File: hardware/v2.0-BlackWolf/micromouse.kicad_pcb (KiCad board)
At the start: 2 copper layers, 100 x 74 mm, 108 parts, among them CN1 6_PIN_HEADER, CN2 6_PIN_HEADER, M1 MOTOR_MOUNTS_AND_ENCODERS, M2 LEFT_MOTOR, M3 2.54MM-SLIDE-SWITCH_TS02_SWIT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, M4 RIGHT_MOTOR, P1 B3B-PH-SM4-TB, P2 B3B-PH-SM4-TB, Q1 DMN3150LW, Q2 DMN3150LW, Q3 DMN3150LW, Q4 DMN3150LW, Q5 TEFT4300, Q6 TEFT4300, Q7 TEFT4300, Q8 TEFT4300, SW1 SWITCH_DPST, SW2 SWITCH_DPST, SW3 SWITCH_DPST, U1 STM32F446RE_LQFP64, U10 MPU-9250, U11 TPS76850, U12 TPS73633, U2 MAX14871, U3 MAX14871, U9 HCMS-2901

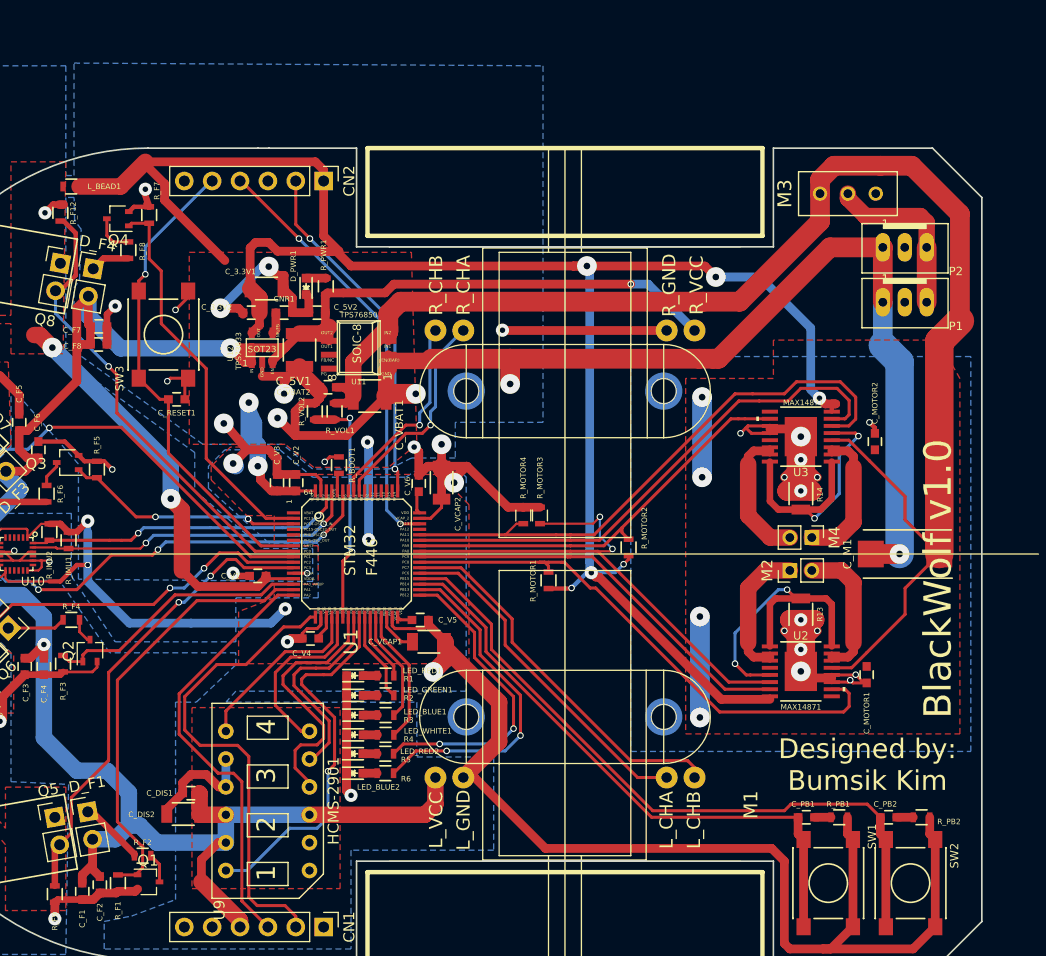
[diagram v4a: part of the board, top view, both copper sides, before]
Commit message: PCB: Separated 5V source due to heat
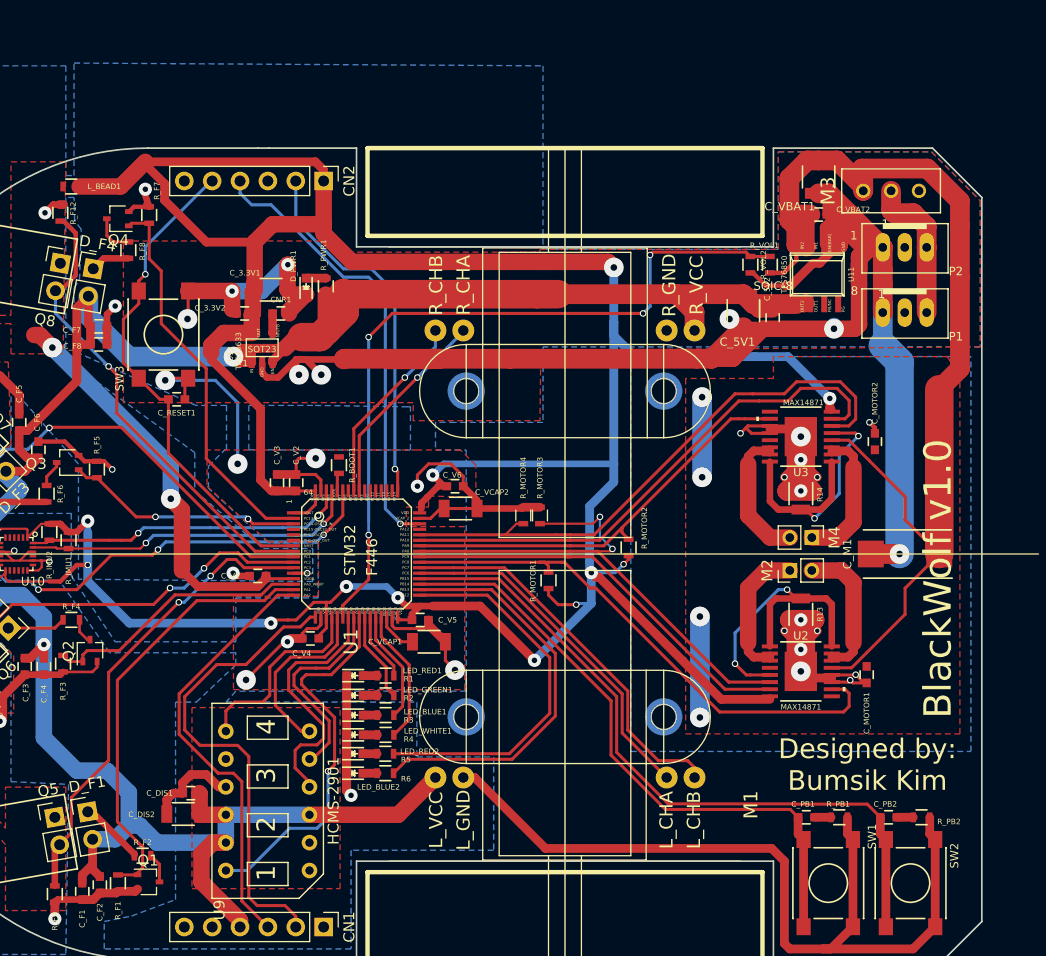
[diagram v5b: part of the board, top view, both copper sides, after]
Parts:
- moved C_VBAT2 47.4 mm to (222.1, 59.1), turned to 0 degrees
- moved C_VBAT1 45.5 mm to (222.1, 55.6), turned to 270 degrees
- moved U11 42.3 mm to (222.0, 64.5), turned to 180 degrees
- moved R_VOL2 41.9 mm to (215.9, 63.6), turned to 270 degrees
- moved R_VOL1 41.9 mm to (217.7, 63.6), turned to 90 degrees
- moved C_5V2 41.5 mm to (217.9, 68.5), turned to 270 degrees
- moved C_5V1 40.6 mm to (215.3, 67.8)
- moved M3 3.95 mm to (228.7, 56.9)
- moved C_V6 3.31 mm to (189.0, 83.8), turned to 0 degrees
- moved C_VCAP2 2.92 mm to (189.5, 85.9), turned to 0 degrees
- moved P1 0.95 mm to (230.0, 67.9)
- moved C_3.3V2 0.61 mm to (169.8, 68.1)
- moved C_3.3V1 0.43 mm to (172.2, 65.9)
- moved CNR1 0.31 mm to (173.1, 68.1)
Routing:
- net +3V3: track 256.2 -> 319.5 mm, vias 11 -> 12
- net BATT_LEVEL: track 21.8 -> 69.7 mm, vias 2 -> 4
- net +BATT: track 139.8 -> 102.7 mm
- net +5V: track 221.8 -> 239.2 mm, vias 3 -> 2
- net GND: track 473.7 -> 486.0 mm, vias 45 -> 42
- net (no net): track 25.6 -> 16.5 mm, vias 6 -> 4
- net LED5: track 28.5 -> 35.1 mm, vias 2 -> 0
- net LED6: track 31.2 -> 37.4 mm, vias 2 -> 0
- net SWDIO: track 39.1 -> 41.6 mm, vias 2 -> 1
- net Net-(M3-PadPIN2): track 15.8 -> 13.5 mm
- net PB1: track 54.8 -> 56.4 mm
- net ~DIS_CE: track 16.4 -> 17.9 mm
- net SWCLK: track 32.1 -> 33.6 mm, vias 2 -> 1
- net RESET: track 44.1 -> 45.3 mm
- net PB2: track 63.0 -> 64.2 mm
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- added copper zone on F.Cu, net GND
- removed copper zone on F.Cu, net +3V3

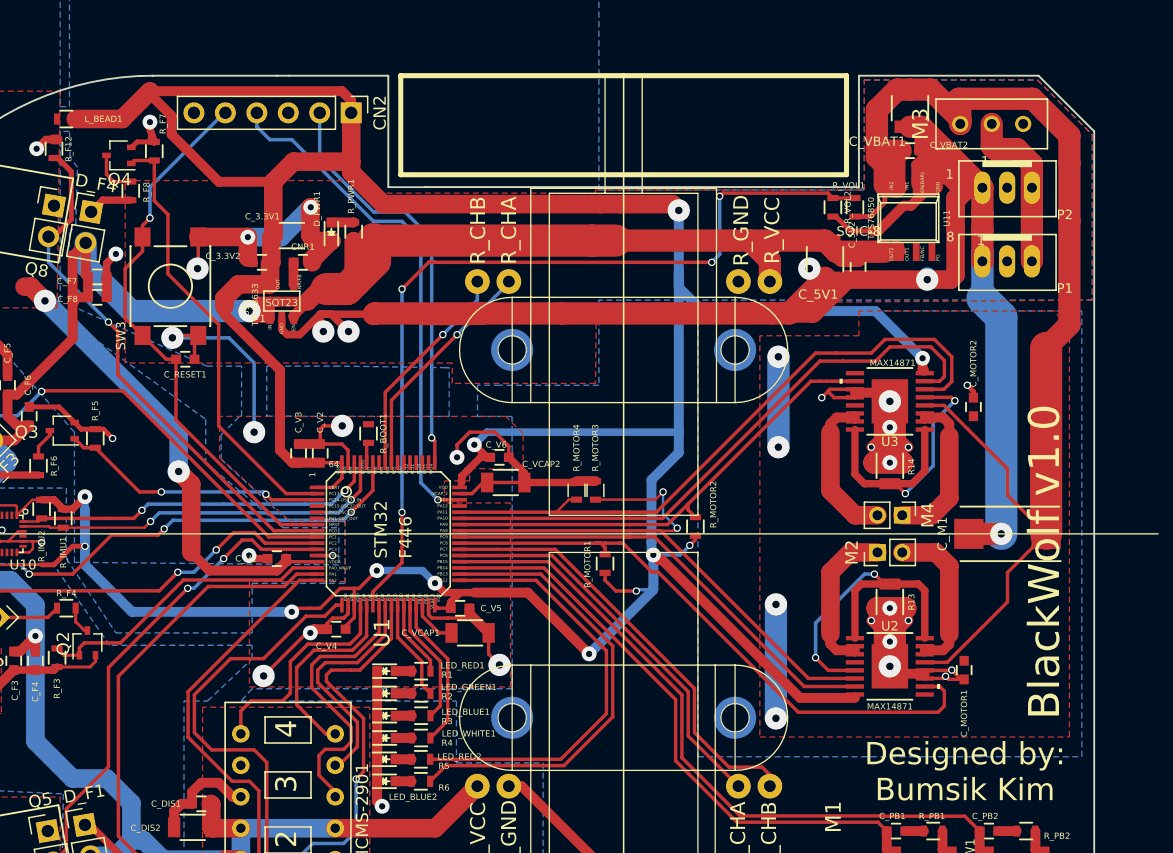
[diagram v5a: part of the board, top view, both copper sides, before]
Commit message: PCB: Added Via Stitching
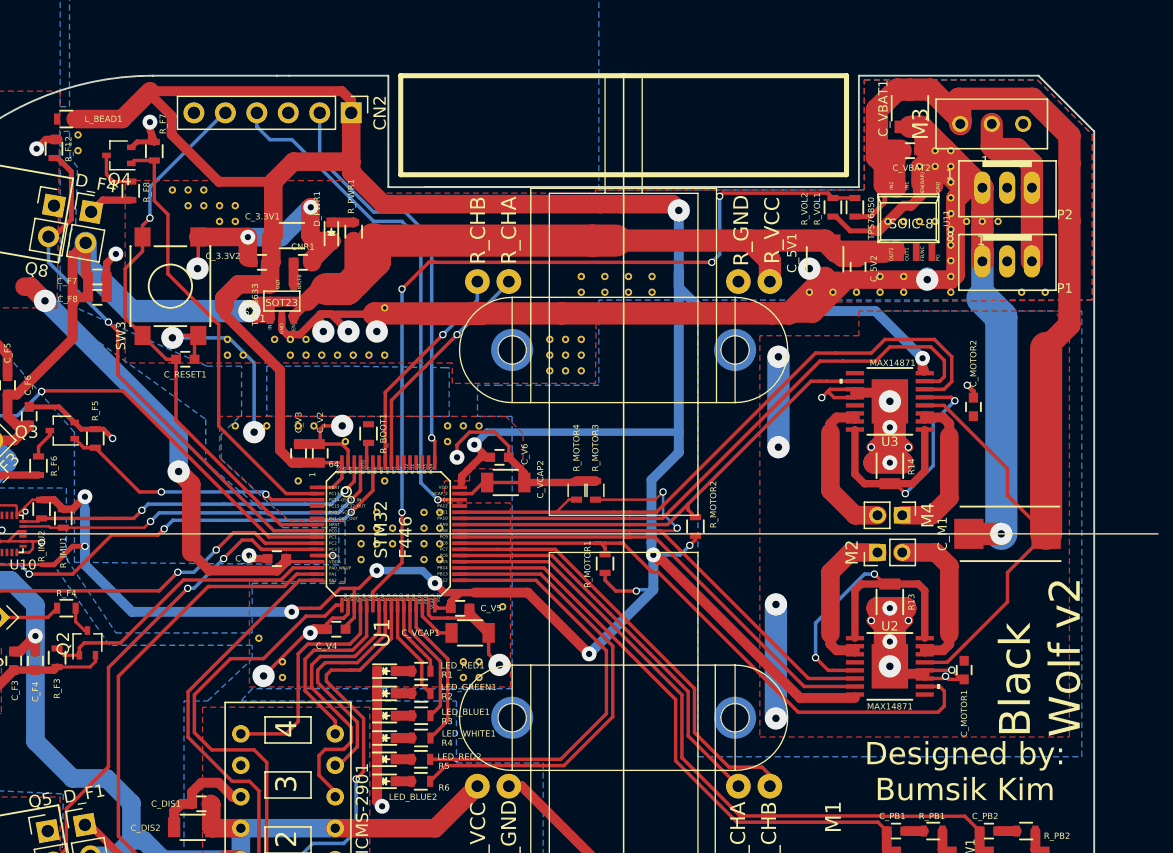
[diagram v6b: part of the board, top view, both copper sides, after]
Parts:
- added VIA_STICH: VIA-0.6mm, footprints_micromouse:VIA-0.6mm, F.Cu at (179.7, 71.8)
- added VIA_STICH: VIA-0.6mm, footprints_micromouse:VIA-0.6mm, F.Cu at (221.6, 64.8)
- added VIA_STICH: VIA-0.6mm, footprints_micromouse:VIA-0.6mm, F.Cu at (179.7, 75.6)
- added VIA_STICH: VIA-0.6mm, footprints_micromouse:VIA-0.6mm, F.Cu at (178.4, 75.6)
- added VIA_STICH: VIA-0.6mm, footprints_micromouse:VIA-0.6mm, F.Cu at (177.2, 75.6)
- added VIA_STICH: VIA-0.6mm, footprints_micromouse:VIA-0.6mm, F.Cu at (175.9, 75.6)
- added VIA_STICH: VIA-0.6mm, footprints_micromouse:VIA-0.6mm, F.Cu at (174.6, 75.6)
- added VIA_STICH: VIA-0.6mm, footprints_micromouse:VIA-0.6mm, F.Cu at (173.4, 75.6)
- added VIA_STICH: VIA-0.6mm, footprints_micromouse:VIA-0.6mm, F.Cu at (172.1, 75.6)
- added VIA_STICH: VIA-0.6mm, footprints_micromouse:VIA-0.6mm, F.Cu at (222.9, 64.8)
- added VIA_STICH: VIA-0.6mm, footprints_micromouse:VIA-0.6mm, F.Cu at (224.2, 64.8)
- added VIA_STICH: VIA-0.6mm, footprints_micromouse:VIA-0.6mm, F.Cu at (225.4, 60.3)
- added VIA_STICH: VIA-0.6mm, footprints_micromouse:VIA-0.6mm, F.Cu at (225.4, 61.6)
- added VIA_STICH: VIA-0.6mm, footprints_micromouse:VIA-0.6mm, F.Cu at (225.4, 62.9)
- added VIA_STICH: VIA-0.6mm, footprints_micromouse:VIA-0.6mm, F.Cu at (225.4, 64.1)
- added VIA_STICH: VIA-0.6mm, footprints_micromouse:VIA-0.6mm, F.Cu at (225.4, 65.4)
- added VIA_STICH: VIA-0.6mm, footprints_micromouse:VIA-0.6mm, F.Cu at (225.4, 66.7)
- added VIA_STICH: VIA-0.6mm, footprints_micromouse:VIA-0.6mm, F.Cu at (225.4, 67.9)
- added VIA_STICH: VIA-0.6mm, footprints_micromouse:VIA-0.6mm, F.Cu at (229.2, 64.8)
- added VIA_STICH: VIA-0.6mm, footprints_micromouse:VIA-0.6mm, F.Cu at (166.4, 64.8)
- added VIA_STICH: VIA-0.6mm, footprints_micromouse:VIA-0.6mm, F.Cu at (167.6, 64.8)
- added VIA_STICH: VIA-0.6mm, footprints_micromouse:VIA-0.6mm, F.Cu at (167.6, 63.5)
- added VIA_STICH: VIA-0.6mm, footprints_micromouse:VIA-0.6mm, F.Cu at (166.4, 63.5)
- added VIA_STICH: VIA-0.6mm, footprints_micromouse:VIA-0.6mm, F.Cu at (163.8, 63.5)
- added VIA_STICH: VIA-0.6mm, footprints_micromouse:VIA-0.6mm, F.Cu at (165.1, 63.5)
- added VIA_STICH: VIA-0.6mm, footprints_micromouse:VIA-0.6mm, F.Cu at (165.1, 62.2)
- added VIA_STICH: VIA-0.6mm, footprints_micromouse:VIA-0.6mm, F.Cu at (163.8, 62.2)
- added VIA_STICH: VIA-0.6mm, footprints_micromouse:VIA-0.6mm, F.Cu at (162.6, 62.2)
- added VIA_STICH: VIA-0.6mm, footprints_micromouse:VIA-0.6mm, F.Cu at (154.9, 59.1)
- added VIA_STICH: VIA-0.6mm, footprints_micromouse:VIA-0.6mm, F.Cu at (228.0, 64.8)
- added VIA_STICH: VIA-0.6mm, footprints_micromouse:VIA-0.6mm, F.Cu at (154.9, 57.8)
- added VIA_STICH: VIA-0.6mm, footprints_micromouse:VIA-0.6mm, F.Cu at (195.6, 69.2)
- added VIA_STICH: VIA-0.6mm, footprints_micromouse:VIA-0.6mm, F.Cu at (197.5, 69.2)
- added VIA_STICH: VIA-0.6mm, footprints_micromouse:VIA-0.6mm, F.Cu at (199.4, 69.2)
- added VIA_STICH: VIA-0.6mm, footprints_micromouse:VIA-0.6mm, F.Cu at (201.3, 69.2)
- added VIA_STICH: VIA-0.6mm, footprints_micromouse:VIA-0.6mm, F.Cu at (195.6, 70.5)
- added VIA_STICH: VIA-0.6mm, footprints_micromouse:VIA-0.6mm, F.Cu at (197.5, 70.5)
- added VIA_STICH: VIA-0.6mm, footprints_micromouse:VIA-0.6mm, F.Cu at (199.4, 70.5)
- added VIA_STICH: VIA-0.6mm, footprints_micromouse:VIA-0.6mm, F.Cu at (201.3, 70.5)
- added VIA_STICH: VIA-0.6mm, footprints_micromouse:VIA-0.6mm, F.Cu at (195.6, 74.3)
- added VIA_STICH: VIA-0.6mm, footprints_micromouse:VIA-0.6mm, F.Cu at (226.7, 64.8)
- added VIA_STICH: VIA-0.6mm, footprints_micromouse:VIA-0.6mm, F.Cu at (195.6, 75.6)
- added VIA_STICH: VIA-0.6mm, footprints_micromouse:VIA-0.6mm, F.Cu at (195.6, 76.8)
- added VIA_STICH: VIA-0.6mm, footprints_micromouse:VIA-0.6mm, F.Cu at (194.3, 76.8)
- added VIA_STICH: VIA-0.6mm, footprints_micromouse:VIA-0.6mm, F.Cu at (194.3, 75.6)
- added VIA_STICH: VIA-0.6mm, footprints_micromouse:VIA-0.6mm, F.Cu at (194.3, 74.3)
- added VIA_STICH: VIA-0.6mm, footprints_micromouse:VIA-0.6mm, F.Cu at (193.0, 74.3)
- added VIA_STICH: VIA-0.6mm, footprints_micromouse:VIA-0.6mm, F.Cu at (193.0, 75.6)
- added VIA_STICH: VIA-0.6mm, footprints_micromouse:VIA-0.6mm, F.Cu at (193.0, 76.8)
- added VIA_STICH: VIA-0.6mm, footprints_micromouse:VIA-0.6mm, F.Cu at (219.7, 69.2)
- added VIA_STICH: VIA-0.6mm, footprints_micromouse:VIA-0.6mm, F.Cu at (221.6, 69.2)
- added VIA_STICH: VIA-0.6mm, footprints_micromouse:VIA-0.6mm, F.Cu at (224.2, 59.1)
- added VIA_STICH: VIA-0.6mm, footprints_micromouse:VIA-0.6mm, F.Cu at (225.4, 69.2)
- added VIA_STICH: VIA-0.6mm, footprints_micromouse:VIA-0.6mm, F.Cu at (233.0, 70.5)
- added VIA_STICH: VIA-0.6mm, footprints_micromouse:VIA-0.6mm, F.Cu at (231.1, 70.5)
- added VIA_STICH: VIA-0.6mm, footprints_micromouse:VIA-0.6mm, F.Cu at (225.4, 70.5)
- added VIA_STICH: VIA-0.6mm, footprints_micromouse:VIA-0.6mm, F.Cu at (214.0, 70.5)
- added VIA_STICH: VIA-0.6mm, footprints_micromouse:VIA-0.6mm, F.Cu at (215.9, 70.5)
- added VIA_STICH: VIA-0.6mm, footprints_micromouse:VIA-0.6mm, F.Cu at (217.8, 70.5)
- added VIA_STICH: VIA-0.6mm, footprints_micromouse:VIA-0.6mm, F.Cu at (219.7, 70.5)
- added VIA_STICH: VIA-0.6mm, footprints_micromouse:VIA-0.6mm, F.Cu at (221.6, 70.5)
- added VIA_STICH: VIA-0.6mm, footprints_micromouse:VIA-0.6mm, F.Cu at (172.7, 85.7)
- added VIA_STICH: VIA-0.6mm, footprints_micromouse:VIA-0.6mm, F.Cu at (225.4, 59.1)
- added VIA_STICH: VIA-0.6mm, footprints_micromouse:VIA-0.6mm, F.Cu at (169.5, 98.4)
- added VIA_STICH: VIA-0.6mm, footprints_micromouse:VIA-0.6mm, F.Cu at (171.4, 100.3)
- added VIA_STICH: VIA-0.6mm, footprints_micromouse:VIA-0.6mm, F.Cu at (171.4, 101.6)
- added VIA_STICH: VIA-0.6mm, footprints_micromouse:VIA-0.6mm, F.Cu at (179.7, 85.7)
- added VIA_STICH: VIA-0.6mm, footprints_micromouse:VIA-0.6mm, F.Cu at (177.8, 92.1)
- added VIA_STICH: VIA-0.6mm, footprints_micromouse:VIA-0.6mm, F.Cu at (179.1, 88.3)
- added VIA_STICH: VIA-0.6mm, footprints_micromouse:VIA-0.6mm, F.Cu at (180.3, 90.8)
- added VIA_STICH: VIA-0.6mm, footprints_micromouse:VIA-0.6mm, F.Cu at (179.1, 90.8)
- added VIA_STICH: VIA-0.6mm, footprints_micromouse:VIA-0.6mm, F.Cu at (177.8, 90.8)
- added VIA_STICH: VIA-0.6mm, footprints_micromouse:VIA-0.6mm, F.Cu at (177.8, 89.5)
- added VIA_STICH: VIA-0.6mm, footprints_micromouse:VIA-0.6mm, F.Cu at (222.9, 60.3)
- added VIA_STICH: VIA-0.6mm, footprints_micromouse:VIA-0.6mm, F.Cu at (179.1, 89.5)
- added VIA_STICH: VIA-0.6mm, footprints_micromouse:VIA-0.6mm, F.Cu at (180.3, 89.5)
- added VIA_STICH: VIA-0.6mm, footprints_micromouse:VIA-0.6mm, F.Cu at (182.9, 92.1)
- added VIA_STICH: VIA-0.6mm, footprints_micromouse:VIA-0.6mm, F.Cu at (182.9, 90.8)
- added VIA_STICH: VIA-0.6mm, footprints_micromouse:VIA-0.6mm, F.Cu at (182.9, 89.5)
- added VIA_STICH: VIA-0.6mm, footprints_micromouse:VIA-0.6mm, F.Cu at (182.9, 88.3)
- added VIA_STICH: VIA-0.6mm, footprints_micromouse:VIA-0.6mm, F.Cu at (184.2, 88.3)
- added VIA_STICH: VIA-0.6mm, footprints_micromouse:VIA-0.6mm, F.Cu at (184.2, 89.5)
- added VIA_STICH: VIA-0.6mm, footprints_micromouse:VIA-0.6mm, F.Cu at (184.2, 90.8)
- added VIA_STICH: VIA-0.6mm, footprints_micromouse:VIA-0.6mm, F.Cu at (184.2, 92.1)
- added VIA_STICH: VIA-0.6mm, footprints_micromouse:VIA-0.6mm, F.Cu at (224.2, 60.3)
- added VIA_STICH: VIA-0.6mm, footprints_micromouse:VIA-0.6mm, F.Cu at (189.2, 95.9)
- added VIA_STICH: VIA-0.6mm, footprints_micromouse:VIA-0.6mm, F.Cu at (186.1, 100.3)
- added VIA_STICH: VIA-0.6mm, footprints_micromouse:VIA-0.6mm, F.Cu at (187.3, 100.3)
- added VIA_STICH: VIA-0.6mm, footprints_micromouse:VIA-0.6mm, F.Cu at (187.3, 101.6)
- added VIA_STICH: VIA-0.6mm, footprints_micromouse:VIA-0.6mm, F.Cu at (186.1, 101.6)
- added VIA_STICH: VIA-0.6mm, footprints_micromouse:VIA-0.6mm, F.Cu at (184.8, 82.5)
- added VIA_STICH: VIA-0.6mm, footprints_micromouse:VIA-0.6mm, F.Cu at (187.3, 81.3)
- added VIA_STICH: VIA-0.6mm, footprints_micromouse:VIA-0.6mm, F.Cu at (186.1, 81.3)
- added VIA_STICH: VIA-0.6mm, footprints_micromouse:VIA-0.6mm, F.Cu at (184.8, 81.3)
- added VIA_STICH: VIA-0.6mm, footprints_micromouse:VIA-0.6mm, F.Cu at (176.5, 82.5)
- added VIA_STICH: VIA-0.6mm, footprints_micromouse:VIA-0.6mm, F.Cu at (220.3, 64.8)
- added VIA_STICH: VIA-0.6mm, footprints_micromouse:VIA-0.6mm, F.Cu at (174.0, 81.3)
- added VIA_STICH: VIA-0.6mm, footprints_micromouse:VIA-0.6mm, F.Cu at (172.7, 81.3)
- added VIA_STICH: VIA-0.6mm, footprints_micromouse:VIA-0.6mm, F.Cu at (170.2, 81.3)
- added VIA_STICH: VIA-0.6mm, footprints_micromouse:VIA-0.6mm, F.Cu at (167.6, 81.3)
- added VIA_STICH: VIA-0.6mm, footprints_micromouse:VIA-0.6mm, F.Cu at (170.8, 74.3)
- added VIA_STICH: VIA-0.6mm, footprints_micromouse:VIA-0.6mm, F.Cu at (173.4, 74.3)
- added VIA_STICH: VIA-0.6mm, footprints_micromouse:VIA-0.6mm, F.Cu at (172.1, 74.3)
- added VIA_STICH: VIA-0.6mm, footprints_micromouse:VIA-0.6mm, F.Cu at (167.0, 74.3)
- added VIA_STICH: VIA-0.6mm, footprints_micromouse:VIA-0.6mm, F.Cu at (168.3, 75.6)
- added VIA_STICH: VIA-0.6mm, footprints_micromouse:VIA-0.6mm, F.Cu at (167.0, 75.6)
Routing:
- net GND: track 486.0 -> 487.5 mm, vias 42 -> 43
- net DIS_SCK: track 16.3 -> 15.3 mm
- net ~DIS_CE: track 17.9 -> 18.5 mm
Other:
- board text added: "Black Wolf v2"
- board text removed: "BlackWolf v1.0"
